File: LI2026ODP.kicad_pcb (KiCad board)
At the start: 4 copper layers, 18.8 x 39.9 mm, 33 parts, among them J1 9-1437539-2, J2 Conn_01x05_Male, U1 LM2936MM-3.3, U2 STM32G0B1KET6, U3 max6921aui

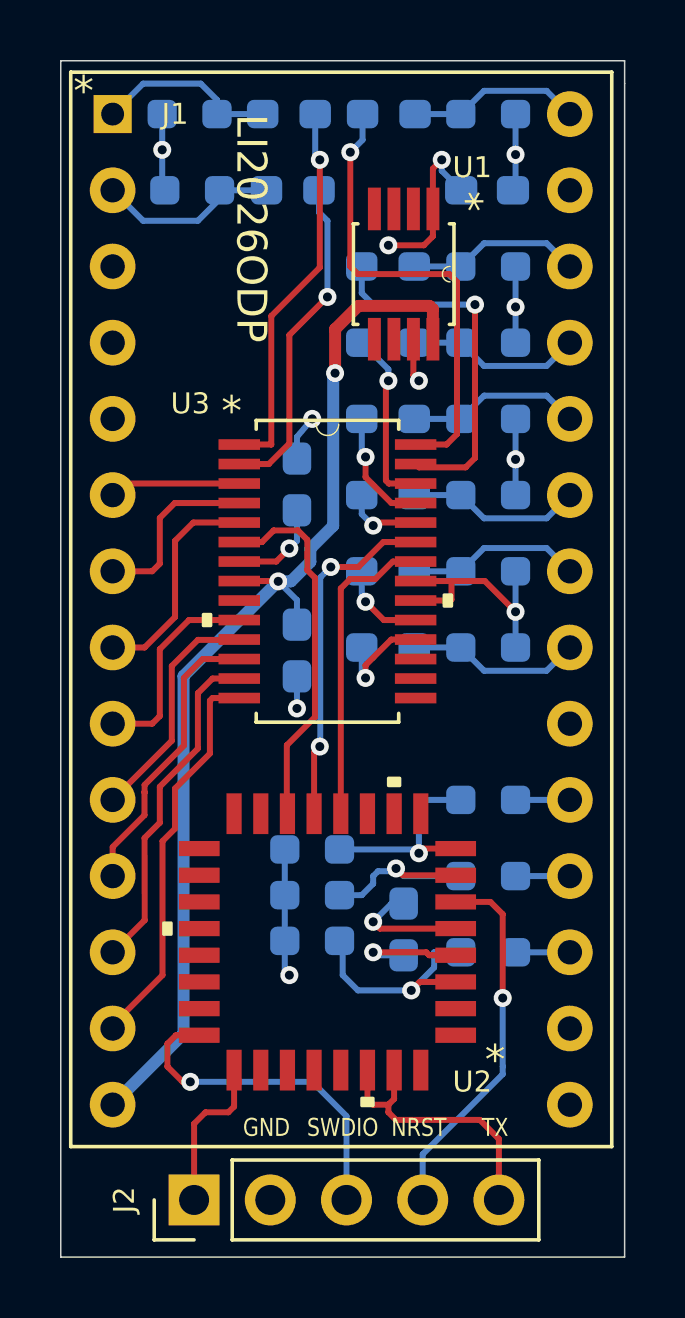
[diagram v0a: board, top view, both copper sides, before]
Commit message: The bypass capacitor layout of the microprocessor is optimized.
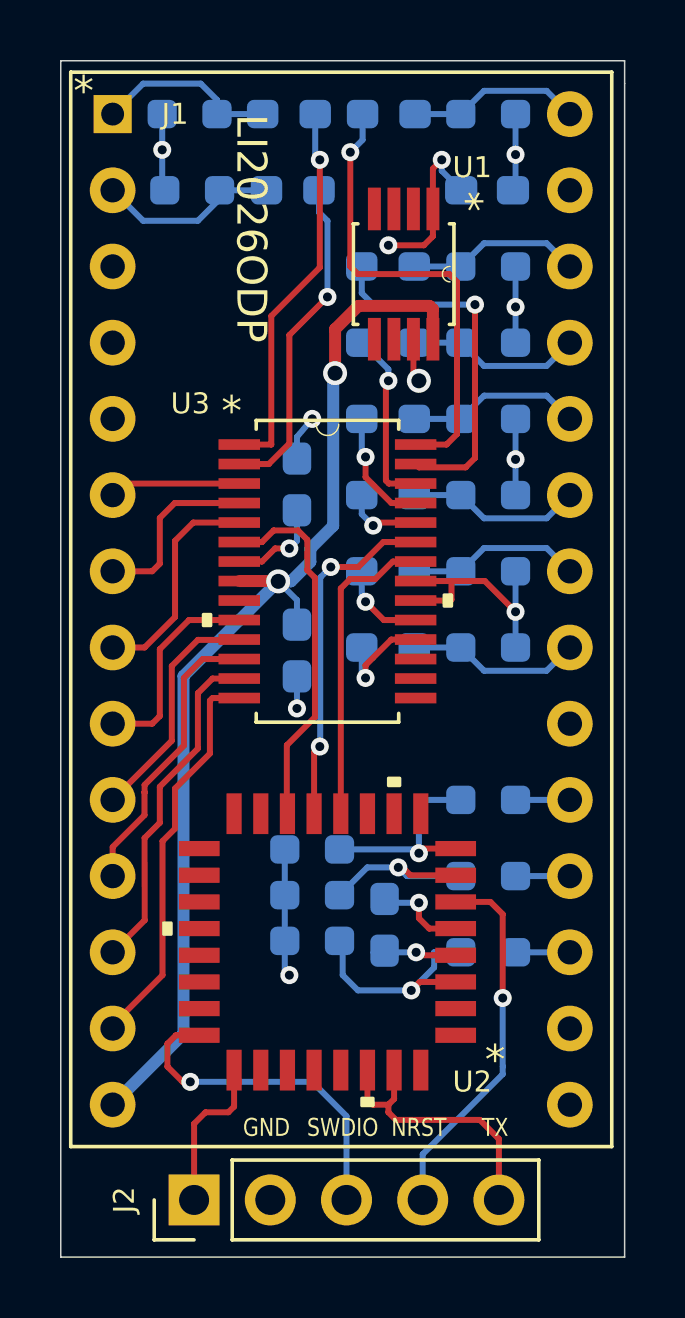
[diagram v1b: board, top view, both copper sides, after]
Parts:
- moved C4 0.65 mm to (126.4, 113.4)
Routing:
- net +3V3: track 12.8 -> 11.5 mm
- net GND: track 30.8 -> 29.7 mm

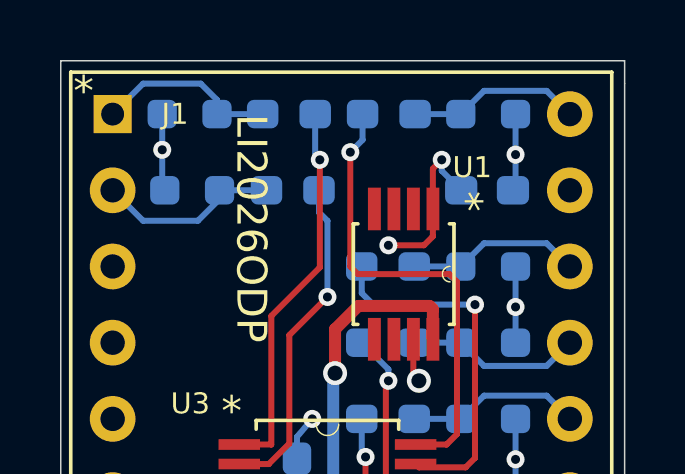
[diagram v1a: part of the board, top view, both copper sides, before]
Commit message: Update C1 from 1608 to 2012
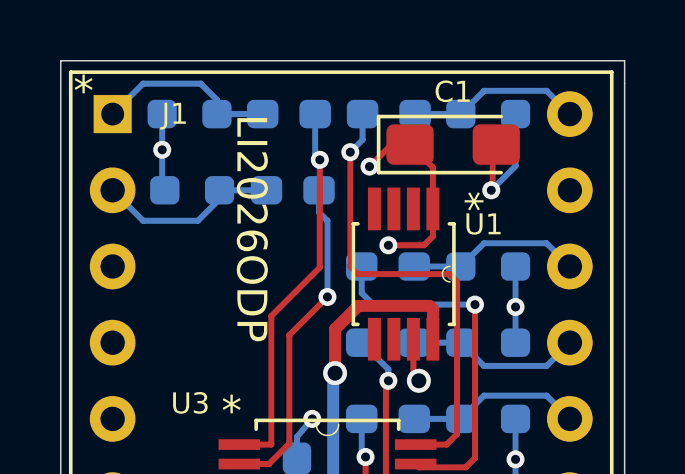
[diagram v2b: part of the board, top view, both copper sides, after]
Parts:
- C1: value 4.7u -> 22uF; footprint Capacitor_SMD:C_0603_1608Metric_Pad1.08x0.95mm_HandSolder -> Capacitor_Tantalum_SMD:CP_EIA-3216-10_Kemet-I_Pad1.58x1.35mm_HandSolder; moved to F.Cu
- moved C1 1.90 mm to (128.7, 87.4)
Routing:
- net GND: track 29.7 -> 31.4 mm
- net +3V3: track 11.5 -> 12.6 mm
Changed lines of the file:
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@@
     (thickness 1.6)
     (drawings 11)
-    (tracks 322)
+    (tracks 323)
     (zones 0)
     (modules 33)
@@
     (0 F.Cu signal)
     (1 In1.Cu power)
-    (2 In2.Cu signal)
+    (2 In2.Cu signal hide)
     (31 B.Cu signal)
     (32 B.Adhes user hide)
@@
     (35 F.Paste user hide)
     (36 B.SilkS user hide)
-    (37 F.SilkS user hide)
+    (37 F.SilkS user)
     (38 B.Mask user hide)
     (39 F.Mask user hide)
@@
     (add_net "Net-(U3-Pad9)")
   )
+  (module Capacitor_Tantalum_SMD:CP_EIA-3216-10_Kemet-I_Pad1.58x1.35mm_HandSolder (layer F.Cu)
+    (at 128.651 87.376)
+    (descr "Tantalum Capacitor SMD Kemet-I (3216-10 Metric), IPC_7351 nominal, (Body size from: http://www.kemet.com/Lists/ProductCatalog/Attachments/253/KEM_TC101_STD.pdf), generated with kicad-footprint-generator")
+    (tags "capacitor tantalum")
+    (attr smd)
+    (fp_text reference C1 (at 0 -1.75) (layer F.SilkS)
+      (effects (font (size 0.7 0.7) (thickness 0.1)))
+    )
+    (fp_text value 22uF (at 0 1.75) (layer F.Fab)
+      (effects (font (size 1 1) (thickness 0.15)))
+    )
+    (fp_text user %R (at 0 0) (layer F.Fab)
+      (effects (font (size 0.8 0.8) (thickness 0.12)))
+    )
+    (fp_line (start 1.6 -0.8) (end -1.2 -0.8) (layer F.Fab) (width 0.1))
+    (fp_line (start -1.2 -0.8) (end -1.6 -0.4) (layer F.Fab) (width 0.1))
+    (fp_line (start -1.6 -0.4) (end -1.6 0.8) (layer F.Fab) (width 0.1))
+    (fp_line (start -1.6 0.8) (end 1.6 0.8) (layer F.Fab) (width 0.1))
+    (fp_line (start 1.6 0.8) (end 1.6 -0.8) (layer F.Fab) (width 0.1))
+    (fp_line (start 1.6 -0.935) (end -2.485 -0.935) (layer F.SilkS) (width 0.12))
+    (fp_line (start -2.485 -0.935) (end -2.485 0.935) (layer F.SilkS) (width 0.12))
+    (fp_line (start -2.485 0.935) (end 1.6 0.935) (layer F.SilkS) (width 0.12))
+    (fp_line (start -2.48 1.05) (end -2.48 -1.05) (layer F.CrtYd) (width 0.05))
+    (fp_line (start -2.48 -1.05) (end 2.48 -1.05) (layer F.CrtYd) (width 0.05))
+    (fp_line (start 2.48 -1.05) (end 2.48 1.05) (layer F.CrtYd) (width 0.05))
+    (fp_line (start 2.48 1.05) (end -2.48 1.05) (layer F.CrtYd) (width 0.05))
+    (pad 2 smd roundrect (at 1.4375 0) (size 1.575 1.35) (layers F.Cu F.Paste F.Mask) (roundrect_rratio 0.185185)
+      (net 27 GND))
+    (pad 1 smd roundrect (at -1.4375 0) (size 1.575 1.35) (layers F.Cu F.Paste F.Mask) (roundrect_rratio 0.185185)
+      (net 28 +3V3))
+    (model ${KISYS3DMOD}/Capacitor_Tantalum_SMD.3dshapes/CP_EIA-3216-10_Kemet-I.wrl
+      (at (xyz 0 0 0))
+      (scale (xyz 1 1 1))
+      (rotate (xyz 0 0 0))
+    )
+  )
   (module Connector_PinHeader_2.54mm:PinHeader_1x05_P2.54mm_Vertical (layer F.Cu)
     (at 120.015 122.555 90)
@@
   (module LM2936MM:LM2936MM-3.3 (layer F.Cu)
     (at 127 91.694 270)
-    (fp_text reference U1 (at -3.556 -2.286 unlocked) (layer F.SilkS)
+    (fp_text reference U1 (at -1.651 -2.667 unlocked) (layer F.SilkS)
       (effects (font (size 0.7 0.7) (thickness 0.1)))
     )
@@
     (pad 1 smd roundrect (at -0.8625 0 270) (size 1.075 0.95) (layers B.Cu B.Paste B.Mask) (roundrect_rratio 0.25)
       (net 29 /+25V))
-    (model ${KISYS3DMOD}/Capacitor_SMD.3dshapes/C_0603_1608Metric.wrl
-      (at (xyz 0 0 0))
-      (scale (xyz 1 1 1))
-      (rotate (xyz 0 0 0))
-    )
-  )
-  (module Capacitor_SMD:C_0603_1608Metric_Pad1.08x0.95mm_HandSolder (layer B.Cu)
-    (at 129.781 88.9)
-    (descr "Capacitor SMD 0603 (1608 Metric), square (rectangular) end terminal, IPC_7351 nominal with elongated pad for handsoldering. (Body size source: IPC-SM-782 page 76, https://www.pcb-3d.com/wordpress/wp-content/uploads/ipc-sm-782a_amendment_1_and_2.pdf), generated with kicad-footprint-generator")
-    (tags "capacitor handsolder")
-    (attr smd)
-    (fp_text reference C1 (at -0.749 1.27) (layer B.SilkS)
-      (effects (font (size 0.7 0.7) (thickness 0.1)) (justify mirror))
-    )
-    (fp_text value 4.7u (at 0 -1.43) (layer B.Fab)
-      (effects (font (size 1 1) (thickness 0.15)) (justify mirror))
-    )
-    (fp_line (start 1.65 -0.73) (end -1.65 -0.73) (layer B.CrtYd) (width 0.05))
-    (fp_line (start 1.65 0.73) (end 1.65 -0.73) (layer B.CrtYd) (width 0.05))
-    (fp_line (start -1.65 0.73) (end 1.65 0.73) (layer B.CrtYd) (width 0.05))
-    (fp_line (start -1.65 -0.73) (end -1.65 0.73) (layer B.CrtYd) (width 0.05))
-    (fp_line (start -0.146267 -0.51) (end 0.146267 -0.51) (layer B.SilkS) (width 0.12))
-    (fp_line (start -0.146267 0.51) (end 0.146267 0.51) (layer B.SilkS) (width 0.12))
-    (fp_line (start 0.8 -0.4) (end -0.8 -0.4) (layer B.Fab) (width 0.1))
-    (fp_line (start 0.8 0.4) (end 0.8 -0.4) (layer B.Fab) (width 0.1))
-    (fp_line (start -0.8 0.4) (end 0.8 0.4) (layer B.Fab) (width 0.1))
-    (fp_line (start -0.8 -0.4) (end -0.8 0.4) (layer B.Fab) (width 0.1))
-    (fp_text user %R (at 0 0) (layer B.Fab)
-      (effects (font (size 0.4 0.4) (thickness 0.06)) (justify mirror))
-    )
-    (pad 2 smd roundrect (at 0.8625 0) (size 1.075 0.95) (layers B.Cu B.Paste B.Mask) (roundrect_rratio 0.25)
-      (net 27 GND))
-    (pad 1 smd roundrect (at -0.8625 0) (size 1.075 0.95) (layers B.Cu B.Paste B.Mask) (roundrect_rratio 0.25)
-      (net 28 +3V3))
     (model ${KISYS3DMOD}/Capacitor_SMD.3dshapes/C_0603_1608Metric.wrl
       (at (xyz 0 0 0))
@@
   (segment (start 118.952 87.55) (end 118.952 88.8135) (width 0.2) (layer B.Cu) (net 27))
   (via (at 118.952 87.55) (size 0.6) (drill 0.3) (layers F.Cu B.Cu) (net 27))
-  (segment (start 130.73 88.8135) (end 130.6435 88.9) (width 0.2) (layer B.Cu) (net 27))
-  (segment (start 130.73 86.36) (end 130.73 87.71) (width 0.2) (layer B.Cu) (net 27))
-  (segment (start 130.73 87.71) (end 130.73 88.8135) (width 0.2) (layer B.Cu) (net 27))
-  (via (at 130.73 87.71) (size 0.6) (drill 0.3) (layers F.Cu B.Cu) (net 27))
   (segment (start 130.73 91.44) (end 130.73 92.79) (width 0.2) (layer B.Cu) (net 27))
   (segment (start 130.73 92.79) (end 130.73 93.98) (width 0.2) (layer B.Cu) (net 27))
@@
   (segment (start 126.492 112.649) (end 126.365 112.522) (width 0.2) (layer B.Cu) (net 27))
   (segment (start 127.508 112.649) (end 126.492 112.649) (width 0.2) (layer B.Cu) (net 27))
+  (via (at 129.921 88.9) (size 0.6) (drill 0.3) (layers F.Cu B.Cu) (net 27))
+  (segment (start 129.966 88.855) (end 129.921 88.9) (width 0.2) (layer F.Cu) (net 27))
+  (segment (start 129.966 87.503) (end 129.966 88.855) (width 0.2) (layer F.Cu) (net 27))
+  (segment (start 130.73 88.091) (end 129.921 88.9) (width 0.2) (layer B.Cu) (net 27))
+  (segment (start 130.73 86.36) (end 130.73 88.091) (width 0.2) (layer B.Cu) (net 27))
   (segment (start 128.63405 114.3) (end 128.73355 114.3995) (width 0.2) (layer F.Cu) (net 28))
   (segment (start 126.0845 114.4005) (end 125.984 114.3) (width 0.2) (layer B.Cu) (net 28))
@@
   (segment (start 123.19 100.838) (end 123.444 100.584) (width 0.2) (layer B.Cu) (net 28))
   (segment (start 123.444 100.584) (end 123.444 99.568) (width 0.2) (layer B.Cu) (net 28))
-  (via (at 128.27 87.884) (size 0.6) (drill 0.3) (layers F.Cu B.Cu) (net 28))
-  (segment (start 127.974999 88.179001) (end 128.27 87.884) (width 0.2) (layer F.Cu) (net 28))
-  (segment (start 127.974999 89.5223) (end 127.974999 88.179001) (width 0.2) (layer F.Cu) (net 28))
-  (segment (start 128.27 88.2515) (end 128.9185 88.9) (width 0.2) (layer B.Cu) (net 28))
-  (segment (start 128.27 87.884) (end 128.27 88.2515) (width 0.2) (layer B.Cu) (net 28))
   (segment (start 127.674997 90.733502) (end 126.492 90.733502) (width 0.2) (layer F.Cu) (net 28))
   (via (at 126.492 90.733502) (size 0.6) (drill 0.3) (layers F.Cu B.Cu) (net 28))
@@
   (segment (start 126.418 114.3) (end 126.365 114.247) (width 0.2) (layer B.Cu) (net 28))
   (segment (start 127.416 114.3) (end 126.418 114.3) (width 0.2) (layer B.Cu) (net 28))
+  (segment (start 127.974999 88.137499) (end 127.2135 87.376) (width 0.2) (layer F.Cu) (net 28))
+  (segment (start 127.974999 89.5223) (end 127.974999 88.137499) (width 0.2) (layer F.Cu) (net 28))
+  (via (at 125.862002 88.110001) (size 0.6) (drill 0.3) (layers F.Cu B.Cu) (net 28))
+  (segment (start 126.596003 87.376) (end 125.862002 88.110001) (width 0.2) (layer F.Cu) (net 28))
+  (segment (start 127.2135 87.376) (end 126.596003 87.376) (width 0.2) (layer F.Cu) (net 28))
   (via (at 122.818707 101.935235) (size 0.8) (drill 0.5) (layers F.Cu B.Cu) (net 29))
   (segment (start 122.80847 101.924998) (end 122.818707 101.935235) (width 0.2) (layer F.Cu) (net 29))

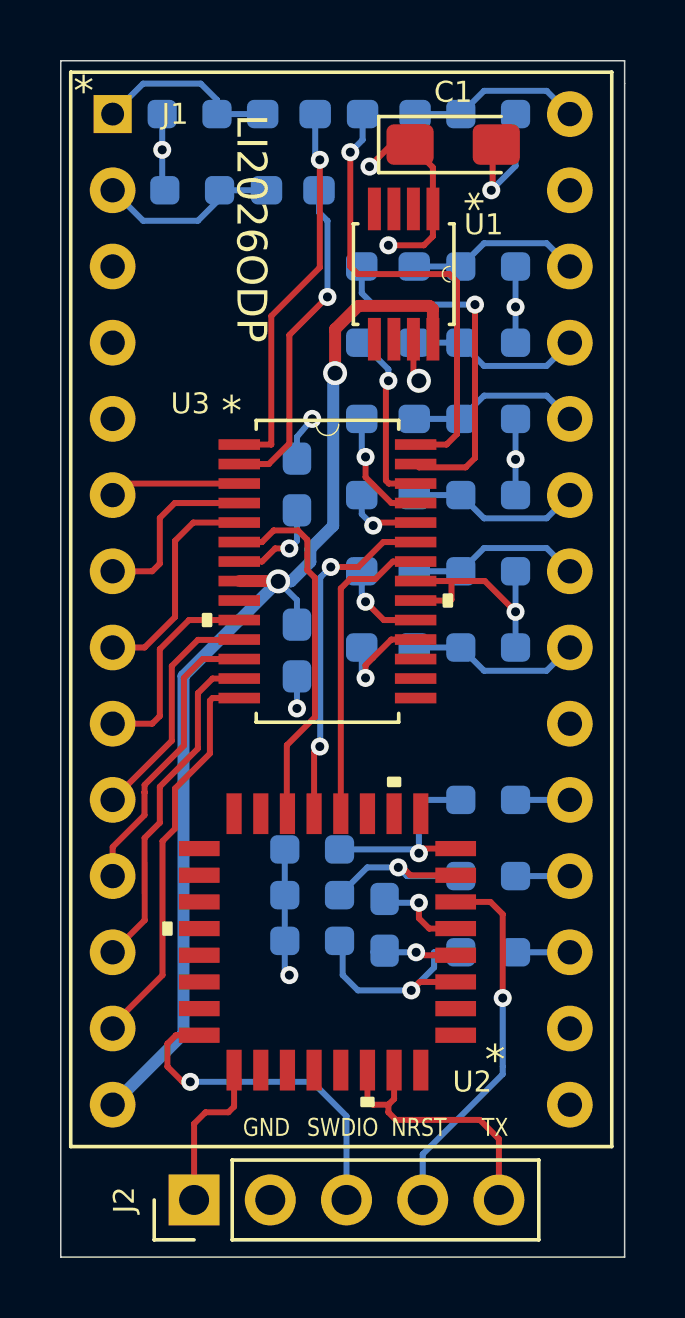
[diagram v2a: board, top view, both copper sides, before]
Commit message: Move LSI's to left
To align them ceter of the board.
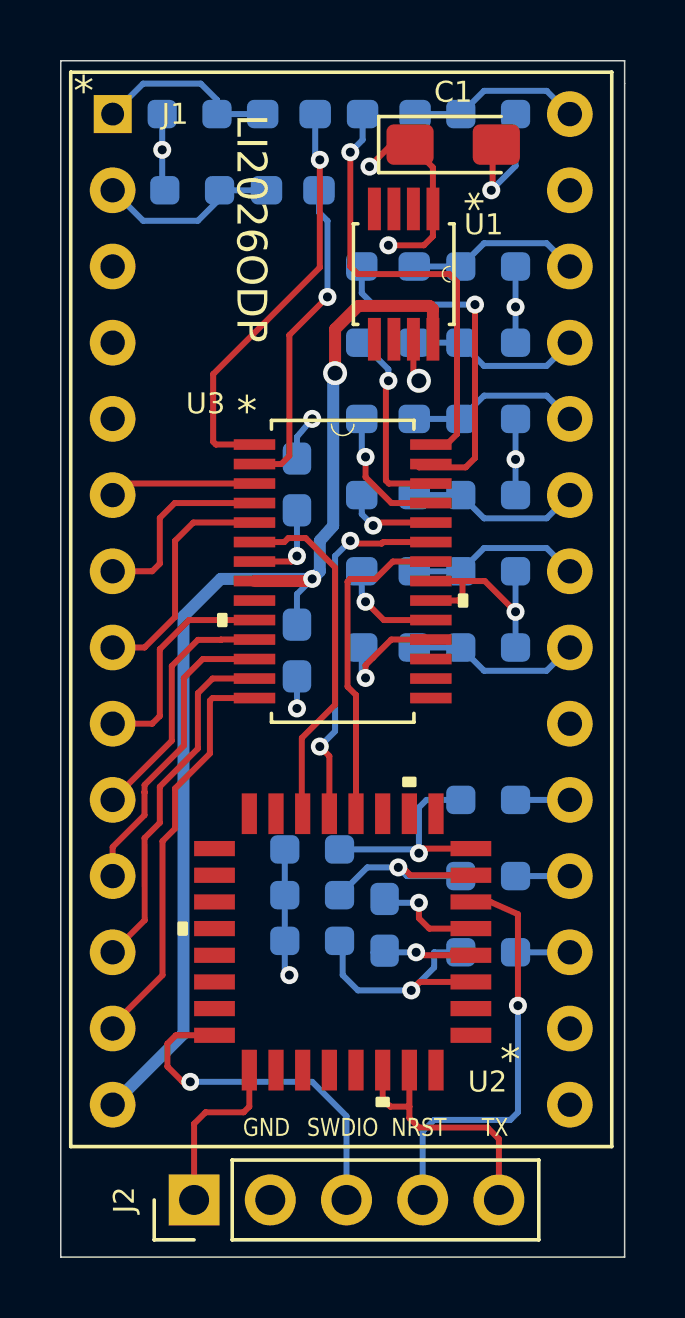
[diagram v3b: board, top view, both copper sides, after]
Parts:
- moved U2 0.51 mm to (125.0, 114.0)
- moved U3 0.51 mm to (125.0, 101.6)
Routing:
- net /+25V: track 36.8 -> 39.1 mm
- net /D1: track 12.8 -> 14.9 mm
- net /NRST: track 12.4 -> 14.5 mm
- net +3V3: track 12.6 -> 14.1 mm
- net /LOAD: track 11.6 -> 12.4 mm
- net /D0: track 11.0 -> 11.8 mm
- net /D8: track 3.52 -> 4.03 mm
- net /SWDIO: track 11.4 -> 11.9 mm
- net /SEG_G: track 6.96 -> 7.46 mm
- net /SEG_F: track 6.06 -> 6.56 mm
- net /SEG_E: track 7.89 -> 8.40 mm
- net /SEG_DP: track 13.3 -> 13.8 mm
- net /SEG_D: track 11.4 -> 11.9 mm
- net /SEG_C: track 9.70 -> 10.2 mm
- net /SEG_B: track 7.43 -> 7.94 mm
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
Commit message: Add capacitor to NRST for noise protection.
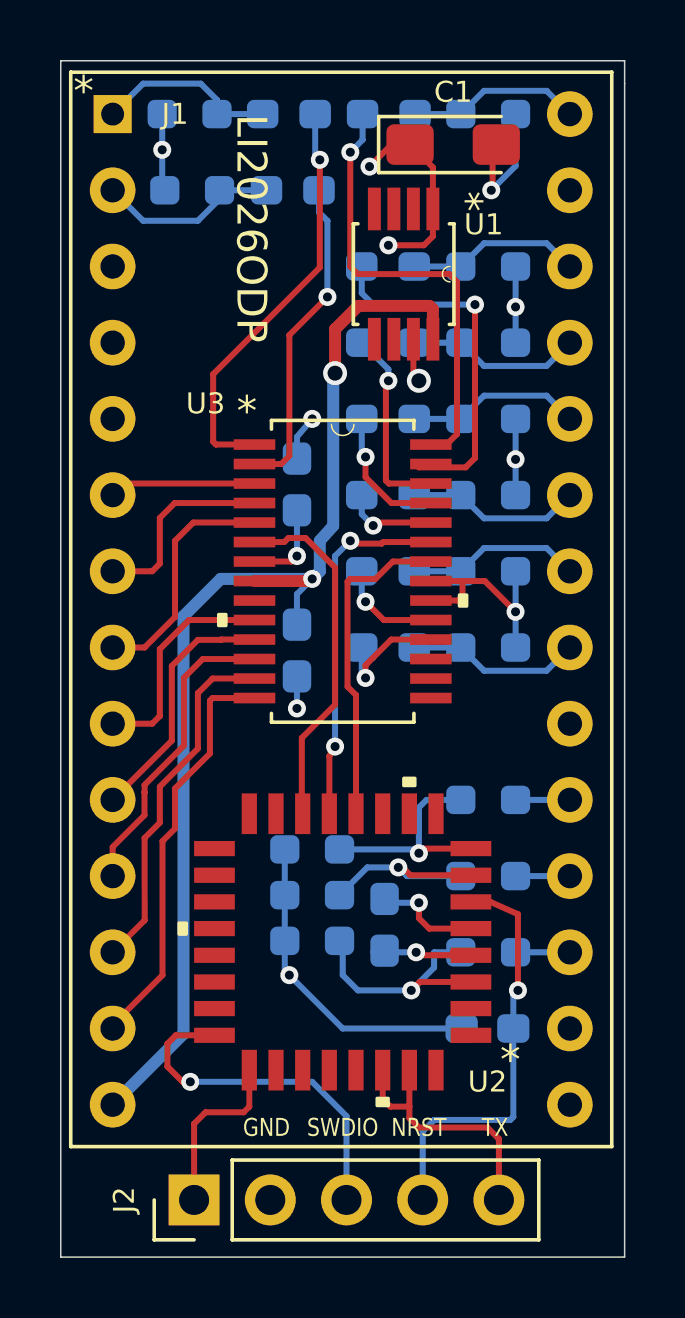
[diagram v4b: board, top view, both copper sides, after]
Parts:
- added C5: 0.1u, Capacitor_SMD:C_0603_1608Metric_Pad1.08x0.95mm_HandSolder, B.Cu at (129.8, 116.8)
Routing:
- net GND: track 31.7 -> 38.2 mm
